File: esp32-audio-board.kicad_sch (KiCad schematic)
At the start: 14 parts, among them J1 USB_C_Receptacle_USB2.0_14P, Q1 SS8050, Q2 SS8050, U1 ESP32-WROOM-32E, U2 CH340C

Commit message: esp32-audio-board: add power supplies
Added the LiPo battery charger and the USB/battery
power switch that will allow the battery to charge
without powering the ESP module. The battery still
powers the audio components while charging.

Added two power LDOs that will supply the ESP32 module
and other functional ICs separate from the audio module.

Signed-off-by: RaresCon <rares.constantin2002@gmail.com>
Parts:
- added C10, C12, C7, C9: 0.1uF, Capacitor_SMD:C_01005_0402Metric_Pad0.57x0.30mm_HandSolder, symbol Device:C
- added C11, C13, C14, C8: 10uF, Capacitor_SMD:C_01005_0402Metric_Pad0.57x0.30mm_HandSolder, symbol Device:C
- added C5, C6: 4.7uF, Capacitor_SMD:C_01005_0402Metric_Pad0.57x0.30mm_HandSolder, symbol Device:C
- added D2: D_Schottky, Diode_SMD:D_3220_8050Metric_Pad2.65x5.15mm_HandSolder, symbol Device:D_Schottky
- added D3: BLUE LED, symbol Device:LED
- added D4: RED LED, symbol Device:LED
- added J2: Conn_01x02_Pin, Connector_JST:JST_PH_S2B-PH-K_1x02_P2.00mm_Horizontal, symbol Connector:Conn_01x02_Pin
- added Q3: 20V/4.2A/52mΩ/1.4W, symbol Simulation_SPICE:PMOS
- added R10, R8: 10K, Resistor_SMD:R_0402_1005Metric_Pad0.72x0.64mm_HandSolder, symbol Device:R_US
- added R11, R7, R9: 1K, Resistor_SMD:R_0402_1005Metric_Pad0.72x0.64mm_HandSolder, symbol Device:R_US
- added R5: 2K, Resistor_SMD:R_0402_1005Metric_Pad0.72x0.64mm_HandSolder, symbol Device:R_US
- added U3: MCP73831-2-OT, Package_TO_SOT_SMD:SOT-23-5, symbol Battery_Management:MCP73831-2-OT
- added U4, U6: LD1117S33TR_SOT223, Package_TO_SOT_SMD:SOT-223-3_TabPin2, symbol Regulator_Linear:LD1117S33TR_SOT223
- renumbered R5 to R6
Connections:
- net +3V3: now also C8.1, C9.1, R10.2, R9.2, U6.2 (VO)
- net GND: now also C10.2, C11.2, C12.2, C13.2, C14.2, C5.2, C6.2, C7.2, C8.2, C9.2, D3.1 (K), D4.1 (K), J2.1 (Pin_1), R5.2, R8.1, U3.2 (V_{SS}), U4.1 (GND), U6.1 (GND)
- net Serial-RX: now also U1.35 (TXD0/IO1)
- net Serial-TX: now also U1.34 (RXD0/IO3)
- net VBUS: now also C5.1, D2.2 (A), Q3.2 (G), R11.1, R7.2, R8.2, U3.4 (V_{DD})
- net at U1.27 (IO16): now also R10.1
- new net: R7.1, U3.1 (STAT)
- new net: D4.2 (A), R11.2
- new net: R5.1, U3.5 (PROG)
- new net: D3.2 (A), R9.1
- new net +3V3 Audio: C12.1, C13.1, U4.2 (VO)
- new net VBAT: C10.1, C14.1, C6.1, J2.2 (Pin_2), Q3.1 (D), U3.3 (V_{BAT}), U4.3 (VI)
- new net VI: C11.1, C7.1, D2.1 (K), Q3.3 (S), U6.3 (VI)
- no-connect marks 5 -> 7
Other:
- note added: "5V-to-3.3V Audio"
- note added: "5V-to-3.3V ESP32"
- note added: "LiPo Battery Charger"
- note added: "Place close to the ES8388 IC"
- note added: "USB/Battery Power Switch"
- moved on the sheet: C2, C3, C4, R6, U1

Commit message: esp32-audio-board: add function buttons
Added four buttons, one for resetting the ESP32 module
and other three for audio functions like volume up/down,
play/pause and next/prev.

Signed-off-by: RaresCon <rares.constantin2002@gmail.com>
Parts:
- removed J1: USB_C_Receptacle_USB2.0_14P, symbol Connector:USB_C_Receptacle_USB2.0_14P
- removed Q3: 20V/4.2A/52mΩ/1.4W, symbol Simulation_SPICE:PMOS
- added C15, C16, C17, C18: 0.1uF, Capacitor_SMD:C_01005_0402Metric_Pad0.57x0.30mm_HandSolder, symbol Device:C
- added J1: EN_PAD0, symbol Connector:Conn_01x01_Pin
- added J10: IO13_PAD1, symbol Connector:Conn_01x01_Pin
- added J3: USB_C_Receptacle_USB2.0_16P, Connector_USB:USB_C_Receptacle_GCT_USB4110, symbol Connector:USB_C_Receptacle_USB2.0_16P
- added J4: EN_PAD1, symbol Connector:Conn_01x01_Pin
- added J5: VP_PAD0, symbol Connector:Conn_01x01_Pin
- added J6: VP_PAD1, symbol Connector:Conn_01x01_Pin
- added J7: VN_PAD0, symbol Connector:Conn_01x01_Pin
- added J8: VN_PAD1, symbol Connector:Conn_01x01_Pin
- added J9: IO13_PAD0, symbol Connector:Conn_01x01_Pin
- added Q4: AO3401A, Package_TO_SOT_SMD:SOT-23_Handsoldering, symbol Transistor_FET:AO3401A
- added R12, R15, R17: 10K, Resistor_SMD:R_0402_1005Metric_Pad0.72x0.64mm_HandSolder, symbol Device:R_US
- added R13, R14, R16: 100R, Resistor_SMD:R_0402_1005Metric_Pad0.72x0.64mm_HandSolder, symbol Device:R_US
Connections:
- net +3V3: now also R12.2, R15.2, R17.2
- net ESP-EN: now also C15.1, J4.1 (Pin_1)
- net ESP-IO0: now also U1.25 (IO0)
- net GND: now also C15.2, C16.2, C17.2, C18.2, J1.1 (Pin_1), J3.A1 (GND), J3.A12 (GND), J3.B1 (GND), J3.B12 (GND), J3.S1 (SHIELD), J5.1 (Pin_1), J7.1 (Pin_1), J9.1 (Pin_1)
- net VBAT: now also Q4.3 (D)
- net VBUS: now also J3.A4 (VBUS), J3.A9 (VBUS), J3.B4 (VBUS), J3.B9 (VBUS), Q4.1 (G)
- net VI: now also Q4.2 (S)
- net at R1.1: now also J3.B5 (CC2)
- net at R2.1: now also J3.A5 (CC1)
- net ESP_IO13: now reaches U1.13 (IO14)
- net ESP_IO13: now also R16.1, R17.1
- net BCK: now reaches U1.29 (IO5)
- net WS: now reaches U1.30 (IO18)
- net DATA_IN: now reaches U1.31 (IO19)
- net DATA_OUT: now reaches U1.33 (IO21)
- net SDA: now reaches U1.36 (IO22)
- net SCL: now reaches U1.37 (IO23)
- net ESP_SENSOR_VP: now reaches U1.4 (SENSOR_VP)
- net ESP_SENSOR_VP: now also R12.1, R13.1
- net ESP_SENSOR_VN: now reaches U1.5 (SENSOR_VN)
- net ESP_SENSOR_VN: now also R14.1, R15.1
- net at U2.5 (UD+): now also J3.A6 (D+), J3.B6 (D+)
- net at U2.6 (UD-): now also J3.A7 (D-), J3.B7 (D-)
- new net: C18.1, J10.1 (Pin_1), R16.2
- new net: C16.1, J6.1 (Pin_1), R13.2
- new net: C17.1, J8.1 (Pin_1), R14.2
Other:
- note added: "Buttons"
- note added: "Espressif's suggestion for IO16 in case of PSRAM"
- note added: "Play/Pause"
- note added: "RESET"
- note added: "USB-UART Bridge"
- note added: "Vol+/Next"
- note added: "Vol-/Previous"
- note removed: "USB-UART"

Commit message: esp32-audio-board: add ES8388 codec
Added the ES8388 codec and all the needed circuits to
allow the user to hook up any speaker they want to some
pads on the PCB.

Signed-off-by: RaresCon <rares.constantin2002@gmail.com>
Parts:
- added C19, C22, C24, C26, C28, C30: 0.1uF, Capacitor_SMD:C_01005_0402Metric_Pad0.57x0.30mm_HandSolder, symbol Device:C
- added C20, C21, C23, C25, C27, C29, C41, C42: 10uF, Capacitor_SMD:C_01005_0402Metric_Pad0.57x0.30mm_HandSolder, symbol Device:C
- added C31, C32, C33, C34, C35: 20pF, Capacitor_SMD:C_01005_0402Metric_Pad0.57x0.30mm_HandSolder, symbol Device:C
- added C36, C37, C38, C39: 22uF, Capacitor_SMD:C_01005_0402Metric_Pad0.57x0.30mm_HandSolder, symbol Device:C
- added C40, C43: 1uF, Capacitor_SMD:C_01005_0402Metric_Pad0.57x0.30mm_HandSolder, symbol Device:C
- added J11: HP_LOUT1, Connector_Wire:SolderWirePad_1x01_SMD_5x10mm, symbol Connector:Conn_01x01_Pin
- added J12: HP_ROUT1, Connector_Wire:SolderWirePad_1x01_SMD_5x10mm, symbol Connector:Conn_01x01_Pin
- added J13: HP_LOUT2, Connector_Wire:SolderWirePad_1x01_SMD_5x10mm, symbol Connector:Conn_01x01_Pin
- added J14: HP_ROUT2, Connector_Wire:SolderWirePad_1x01_SMD_5x10mm, symbol Connector:Conn_01x01_Pin
- added J15: MIC_LIN1, Connector_Wire:SolderWirePad_1x01_SMD_5x10mm, symbol Connector:Conn_01x01_Pin
- added J16: MIC_LIN1_GND, Connector_Wire:SolderWirePad_1x01_SMD_5x10mm, symbol Connector:Conn_01x01_Pin
- added J17: MIC_RIN1, Connector_Wire:SolderWirePad_1x01_SMD_5x10mm, symbol Connector:Conn_01x01_Pin
- added J18: MIC_RIN1_GND, Connector_Wire:SolderWirePad_1x01_SMD_5x10mm, symbol Connector:Conn_01x01_Pin
- added J19: HP_1GND, Connector_Wire:SolderWirePad_1x01_SMD_5x10mm, symbol Connector:Conn_01x01_Pin
- added J20: HP_2GND, Connector_Wire:SolderWirePad_1x01_SMD_5x10mm, symbol Connector:Conn_01x01_Pin
- added R18: 4.7R, Resistor_SMD:R_0402_1005Metric_Pad0.72x0.64mm_HandSolder, symbol Device:R_US
- added R19, R20, R21: 100R, Resistor_SMD:R_0402_1005Metric_Pad0.72x0.64mm_HandSolder, symbol Device:R_US
- added R22, R23, R33, R35: 2K, Resistor_SMD:R_0402_1005Metric_Pad0.72x0.64mm_HandSolder, symbol Device:R_US
- added R24, R25, R26, R27, R28, R29, R30, R31, R32: 33R, Resistor_SMD:R_0402_1005Metric_Pad0.72x0.64mm_HandSolder, symbol Device:R_US
- added R34, R36: 1K, Resistor_SMD:R_0402_1005Metric_Pad0.72x0.64mm_HandSolder, symbol Device:R_US
- added U5: ES8388, Package_DFN_QFN:QFN-28-1EP_4x4mm_P0.45mm_EP2.6x2.6mm, symbol ES8388:ES8388
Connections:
- net +3V3 Audio: now also C19.1, C20.1, C29.1, R18.2, R19.1, R22.1, R23.1, R34.2, R36.2, U5.16 (HPVDD)
- net BCK: now also R25.1
- net DATA_IN: now also R28.1
- net DATA_OUT: now also R27.1
- net ESP-IO0: now also R24.1
- net GND: now also C19.2, C20.2, C21.2, C22.2, C23.2, C24.2, C25.2, C26.2, C27.2, C28.2, C29.2, C30.2, C31.2, C32.2, C33.2, C34.2, C35.2, C41.1, C42.1, J16.1 (Pin_1), J18.1 (Pin_1), J19.1 (Pin_1), J20.1 (Pin_1), U5.13 (HPGND), U5.18 (AGND), U5.26 (CE), U5.29 (PGND), U5.4 (DGND)
- net SCL: now also R20.1, R22.2
- net SDA: now also R21.1, R23.2
- net WS: now also R26.1
- net ESP_IO13 renamed ESP_IO14
- new net: C31.1, R21.2, U5.27 (CDATA)
- new net: C43.2, J17.1 (Pin_1), R35.1
- new net: C42.2, R35.2, R36.1
- new net: C21.1, C22.1, R18.1, U5.17 (AVDD)
- new net: C39.2, R32.1
- new net: J14.1 (Pin_1), R32.2
- new net: C30.1, R19.2, U5.2 (DVDD), U5.3 (PVDD)
- new net: C32.1, R20.2, U5.28 (CCLK)
- new net: R27.2, U5.6 (DSDIN)
- new net: R28.2, U5.8 (ASDOUT)
- new net: C40.2, J15.1 (Pin_1), R33.1
- new net: C41.2, R33.2, R34.1
- new net: C38.2, R31.1
- new net: J13.1 (Pin_1), R31.2
- new net: J11.1 (Pin_1), R30.2
- new net: J12.1 (Pin_1), R29.2
- new net: C37.2, R29.1
- new net: C36.2, R30.1
- new net ES8388_ADCVREF: C25.1, C26.1, U5.19 (ADCVREF)
- new net ES8388_LIN1: C40.1, U5.24 (LIN1)
- new net ES8388_LOUT1: C36.1, U5.12 (LOUT1)
- new net ES8388_LOUT2: C38.1, U5.15 (LOUT2)
- new net ES8388_LRCK: C35.1, R26.2, U5.7 (LRCK)
- new net ES8388_MCLK: C33.1, R24.2, U5.1 (MCLK)
- new net ES8388_RIN1: C43.1, U5.23 (RIN1)
- new net ES8388_ROUT1: C37.1, U5.11 (ROUT1)
- new net ES8388_ROUT2: C39.1, U5.14 (ROUT2)
- new net ES8388_SCLK: C34.1, R25.2, U5.5 (SCLK)
- new net ES8388_VMID: C23.1, C24.1, U5.20 (VMID)
- new net ES8388_VREF: C27.1, C28.1, U5.10 (VREF)
- no-connect marks 7 -> 9
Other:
- note added: "Audio circuits"
- note added: "Default addr: 0x20"
- note added: "Place these as close as possible to the ES8388 codec"
- note added: "Place these together on the PCB to allow the user to connect the speaker in the same place"
- moved on the sheet: D2, Q4, R8

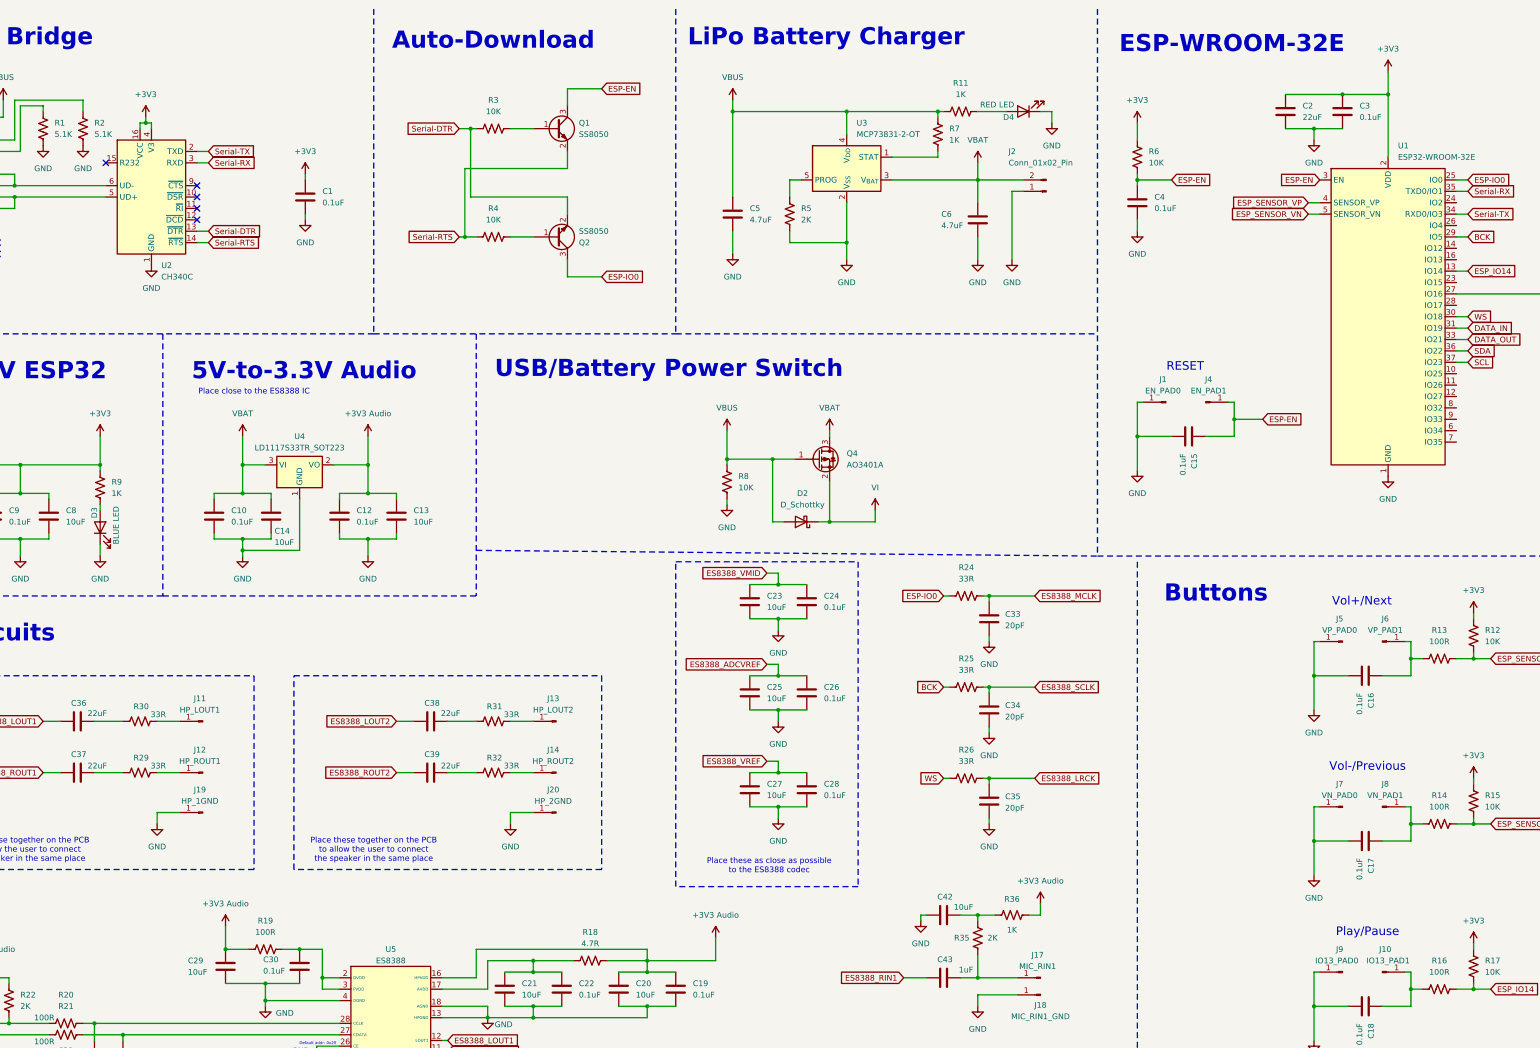
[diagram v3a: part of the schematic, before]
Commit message: esp32-audio-board: small improvements
Added some small improvements on the schematic to be easier
to understand before continuing to PCB design.

Signed-off-by: RaresCon <rares.constantin2002@gmail.com>
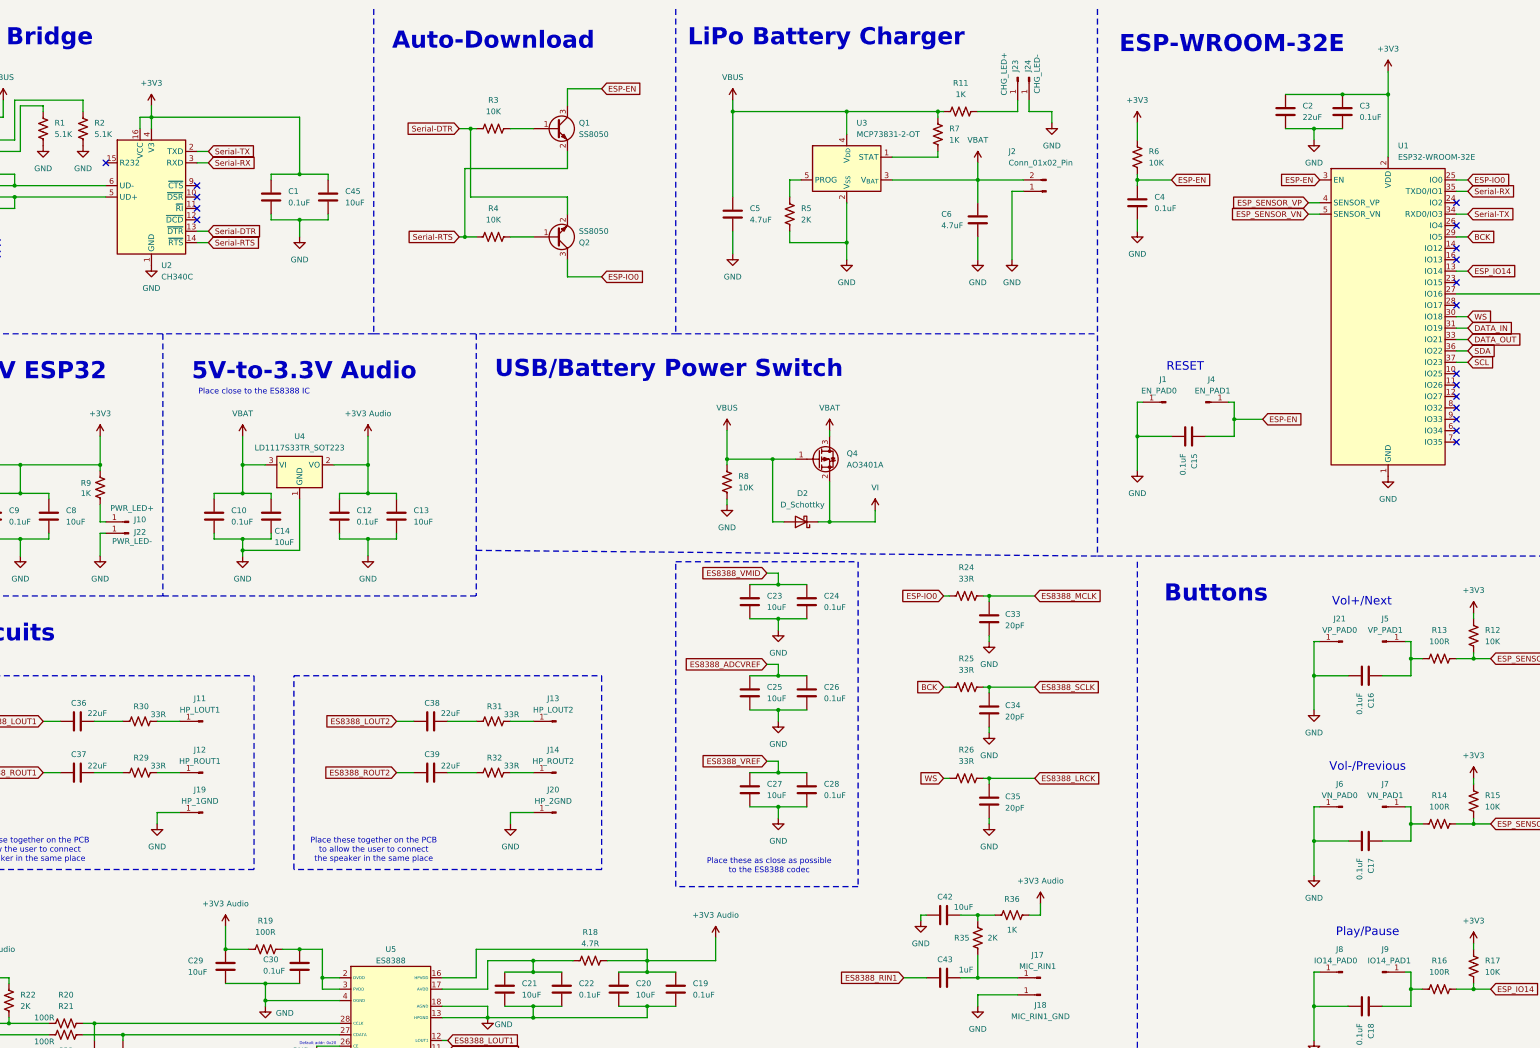
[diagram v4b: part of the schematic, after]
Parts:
- removed D3: BLUE LED, symbol Device:LED
- removed D4: RED LED, symbol Device:LED
- added C45: 10uF, Capacitor_SMD:C_01005_0402Metric_Pad0.57x0.30mm_HandSolder, symbol Device:C
- added J21: VP_PAD0, Connector_Wire:SolderWirePad_1x01_SMD_5x10mm, symbol Connector:Conn_01x01_Pin
- added J22: PWR_LED-, Connector_Wire:SolderWirePad_1x01_SMD_5x10mm, symbol Connector:Conn_01x01_Pin
- added J23: CHG_LED+, Connector_Wire:SolderWirePad_1x01_SMD_5x10mm, symbol Connector:Conn_01x01_Pin
- added J24: CHG_LED-, Connector_Wire:SolderWirePad_1x01_SMD_5x10mm, symbol Connector:Conn_01x01_Pin
- J1, J4: footprint (none) -> Connector_Wire:SolderWirePad_1x01_SMD_5x10mm
- J10: value IO13_PAD1 -> PWR_LED+; footprint (none) -> Connector_Wire:SolderWirePad_1x01_SMD_5x10mm
- J5: value VP_PAD0 -> VP_PAD1; footprint (none) -> Connector_Wire:SolderWirePad_1x01_SMD_5x10mm
- J6: value VP_PAD1 -> VN_PAD0; footprint (none) -> Connector_Wire:SolderWirePad_1x01_SMD_5x10mm
- J7: value VN_PAD0 -> VN_PAD1; footprint (none) -> Connector_Wire:SolderWirePad_1x01_SMD_5x10mm
- J8: value VN_PAD1 -> IO14_PAD0; footprint (none) -> Connector_Wire:SolderWirePad_1x01_SMD_5x10mm
- J9: value IO13_PAD0 -> IO14_PAD1; footprint (none) -> Connector_Wire:SolderWirePad_1x01_SMD_5x10mm
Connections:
- net +3V3: now also C45.1
- net GND: now also J6.1 (Pin_1), J8.1 (Pin_1), C45.2, J21.1 (Pin_1), J22.1 (Pin_1), J24.1 (Pin_1); no longer J5.1 (Pin_1), J7.1 (Pin_1), J9.1 (Pin_1)
- net at C18.1, R16.2: now also J9.1 (Pin_1); no longer J10.1 (Pin_1)
- net at C16.1, R13.2: now also J5.1 (Pin_1); no longer J6.1 (Pin_1)
- net at R11.2: now also J23.1 (Pin_1)
- net at C17.1, R14.2: now also J7.1 (Pin_1); no longer J8.1 (Pin_1)
- net at R9.1: now also J10.1 (Pin_1)
- no-connect marks 9 -> 22

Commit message: esp32-audio-board: PCB design and change LDOs
Added the initial position of the components on the board,
the button and input pads need to be placed on the outer
part of the PCB.

Changed the LDOs to XC6220A331 to allow for a lower DO
voltage, which would occur while using the battery.

Signed-off-by: RaresCon <rares.constantin2002@gmail.com>
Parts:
- removed U4, U6: LD1117S33TR_SOT223, Package_TO_SOT_SMD:SOT-223-3_TabPin2, symbol Regulator_Linear:LD1117S33TR_SOT223
- added H1, H2, H3, H4: MountingHole_Pad, MountingHole:MountingHole_2.2mm_M2_Pad_TopOnly, symbol Mechanical:MountingHole_Pad
- added IC1, IC2: XC6220A331MR-G, xc6220a331:SOT95P280X120-5N, symbol XC6220A331MR-G:XC6220A331MR-G
- added R37, R38: 100K, Resistor_SMD:R_0402_1005Metric_Pad0.72x0.64mm_HandSolder, symbol Device:R_US
- C1, C10, C11, C12, C13, C14, C15, C16, C17, C18, C19, C2, C20, C21, C22, C23, C24, C25, C26, C27, C28, C29, C3, C30, C31, C32, C33, C34, C35, C36, C37, C38, C39, C4, C40, C41, C42, C43, C45, C5, C6, C7, C8, C9: footprint Capacitor_SMD:C_01005_0402Metric_Pad0.57x0.30mm_HandSolder -> Capacitor_SMD:C_0402_1005Metric_Pad0.74x0.62mm_HandSolder
- J1, J10, J11, J12, J13, J14, J15, J16, J17, J18, J19, J20, J21, J22, J23, J24, J4, J5, J6, J7, J8, J9: footprint Connector_Wire:SolderWirePad_1x01_SMD_5x10mm -> Connector_Wire:SolderWirePad_1x01_SMD_1x2mm
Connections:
- net +3V3: now also IC1.5 (VOUT)
- net +3V3 Audio: now also IC2.5 (VOUT)
- net GND: now also H1.1, H2.1, H3.1, H4.1, IC1.2 (VSS), IC2.2 (VSS), R38.2
- net VBAT: now also IC2.1 (VIN), IC2.3 (CE), R37.1
- net VI: now also IC1.1 (VIN), IC1.3 (CE)
- net BAT_LVL: now reaches U1.6 (IO34)
- net BAT_LVL: now also R37.2, R38.1
- no-connect marks 22 -> 21
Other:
- note added: "Battery Monitor"
- note added: "MHs"
- note added: "Power Switch"
- note removed: "USB/Battery Power Switch"
- moved on the sheet: C10, C12, C13, C14, C8, C9, D2, J10, J22, Q4, R8, R9
